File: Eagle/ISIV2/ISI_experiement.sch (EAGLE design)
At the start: 59 parts, among them IC1 74AC11374D, IC3 74AC11374D, IC4 74AC11374D, IC5 74266D, IC6 74266D, IC7 74HC04D

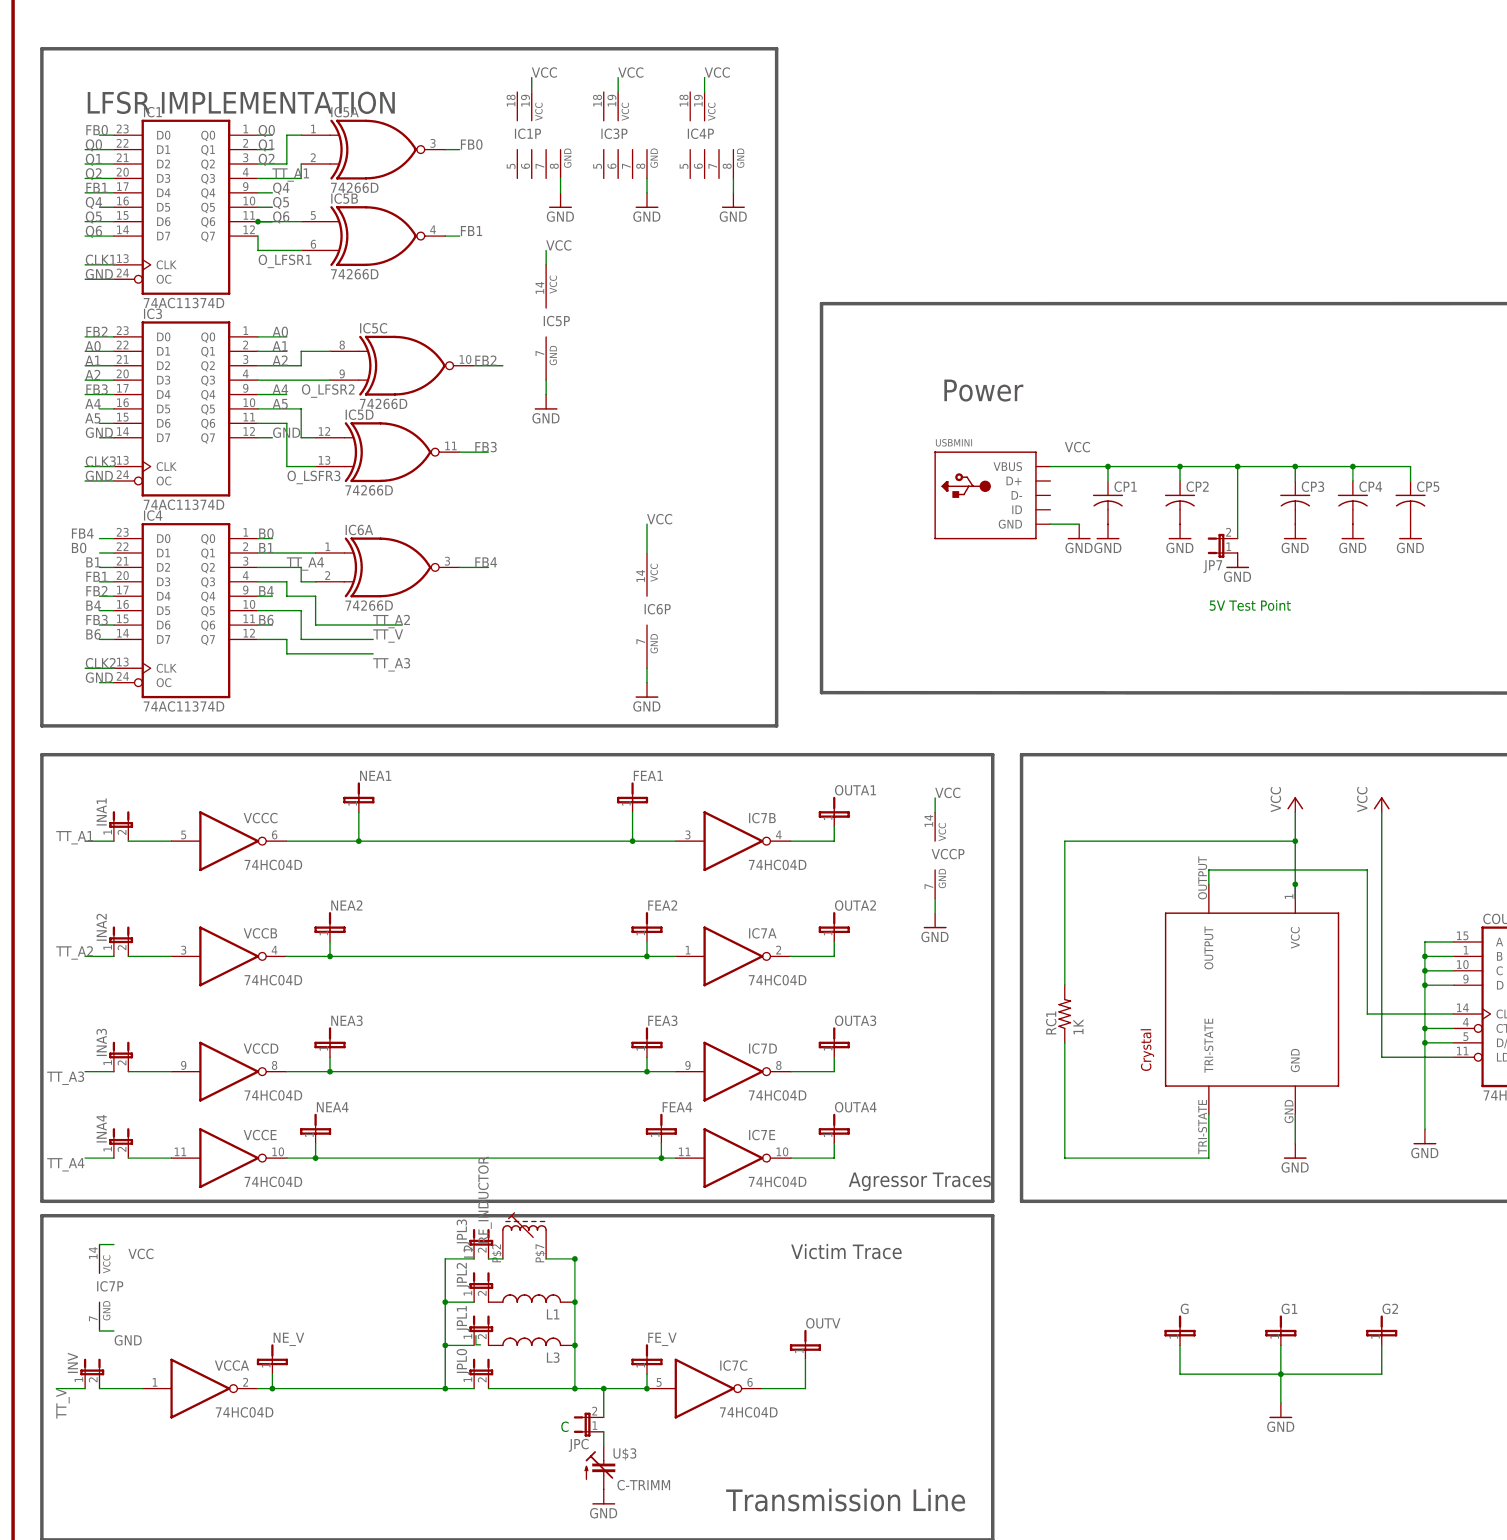
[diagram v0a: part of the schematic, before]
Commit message: ISI with test points
added test point to near and far end of TL
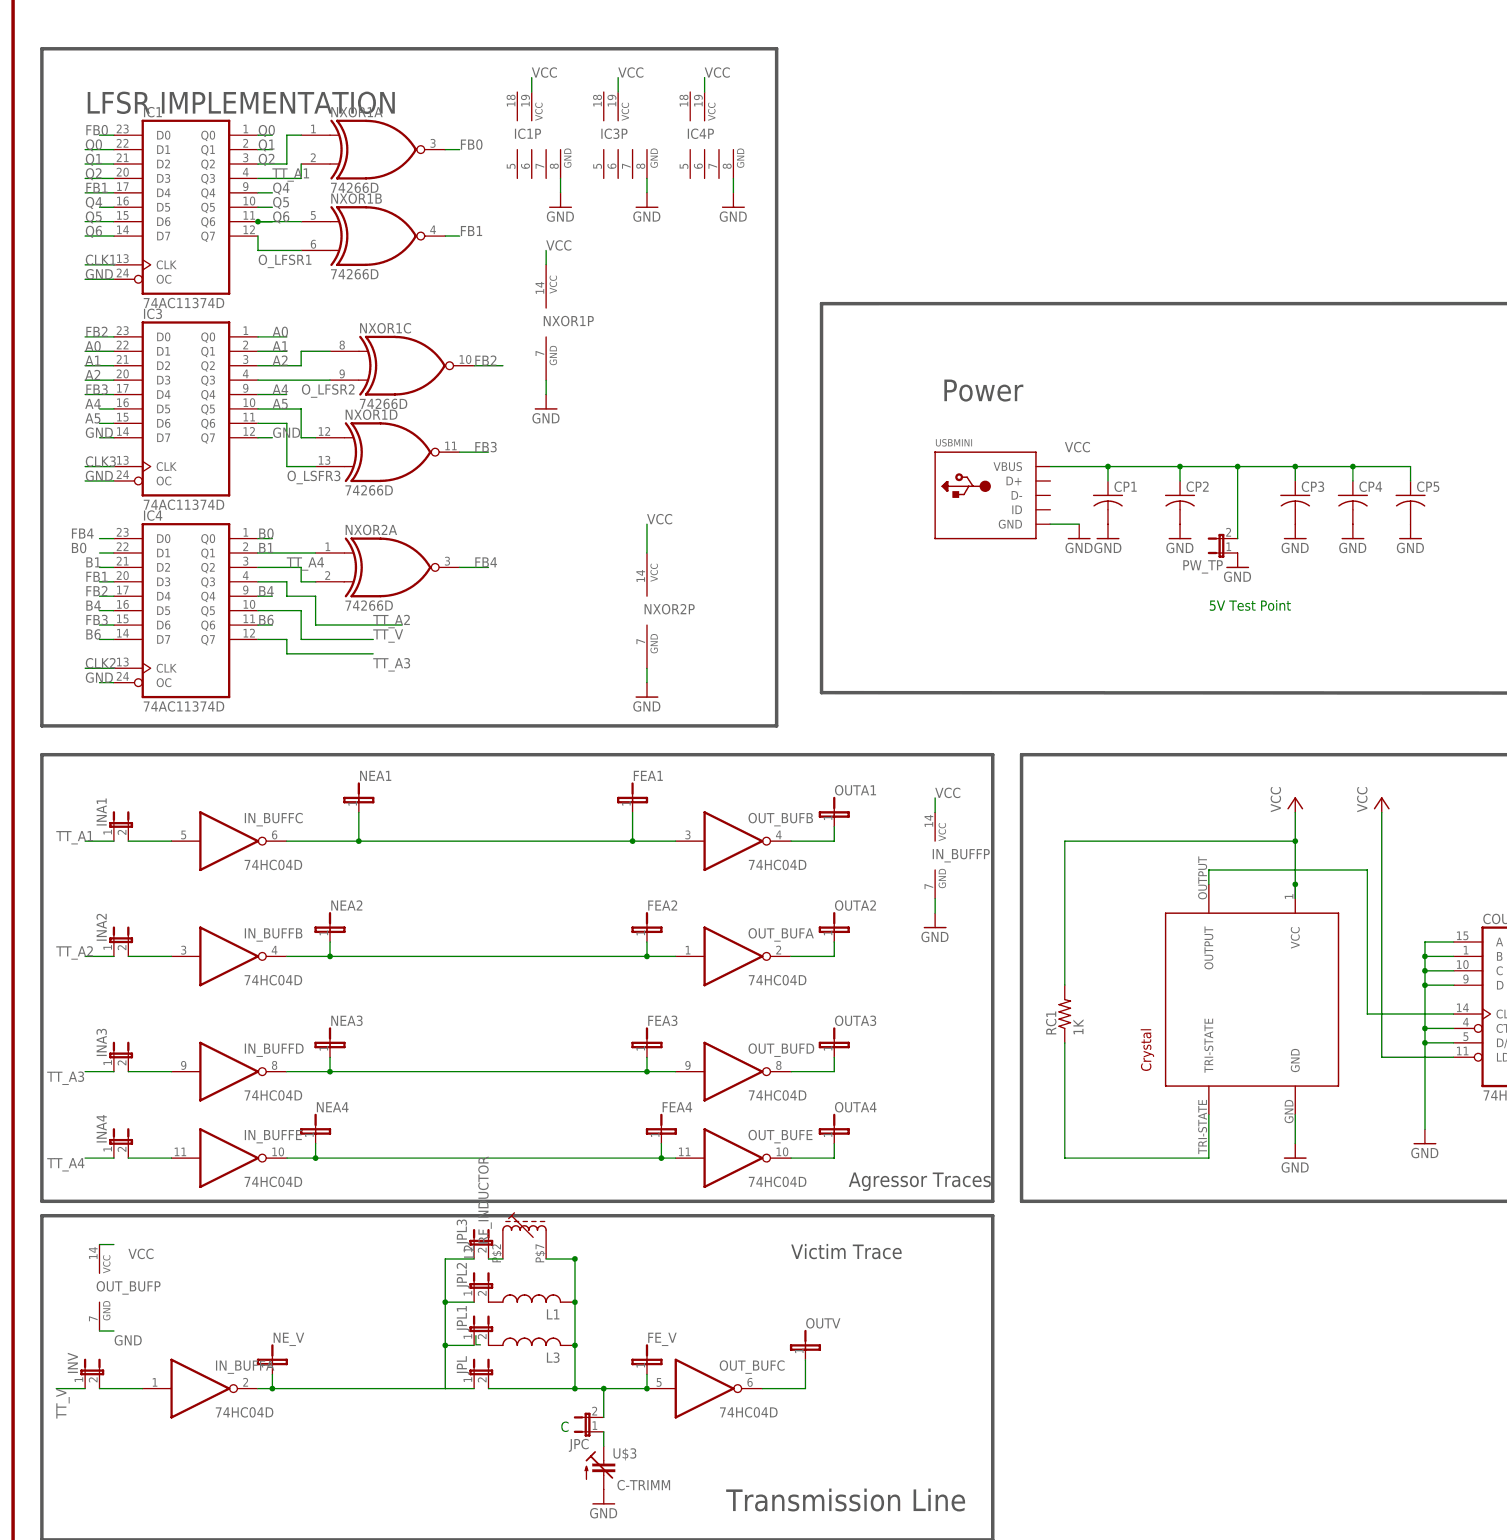
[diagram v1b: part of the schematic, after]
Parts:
- removed G, G1, G2: JP1, E3VB_ISI:JP1
- renumbered IC5 to NXOR1, IC6 to NXOR2, IC7 to OUT_BUF, JP7 to PW_TP, JPL0 to JPL, VCC to IN_BUFF
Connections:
- net GND: no longer G.1, G1.1, G2.1
